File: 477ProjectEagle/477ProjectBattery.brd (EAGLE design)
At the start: 100 x 80 mm, 21 parts

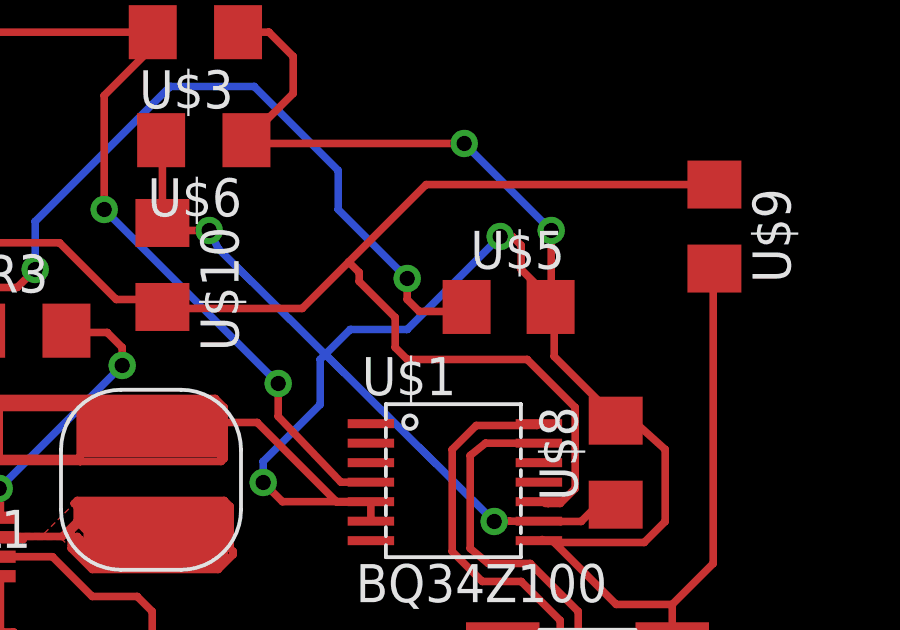
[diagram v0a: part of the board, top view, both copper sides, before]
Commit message: Made Major changes to the Battery PCB
I finished up the Battery PCB and incorporated the recommended layout
for the 3.3V source.
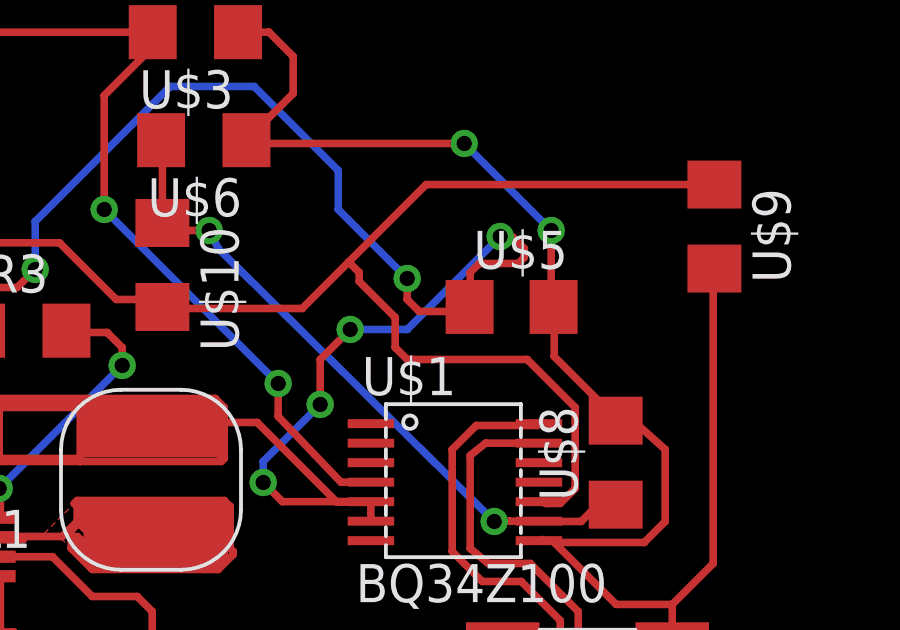
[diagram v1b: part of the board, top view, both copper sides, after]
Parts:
- moved U$5 0.10 mm to (58.6, 46.2)
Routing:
- net +3V3: track 134.6 -> 135.7 mm, vias 4 -> 6
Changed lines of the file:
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@@
 <element name="U$3" library="MinotaurParts" package="R1206" value="16k" x="48.04" y="55.41" rot="R180"/>
 <element name="U$4" library="MinotaurParts" package="R1206" value="240k" x="35.46" y="52.01" rot="R180"/>
-<element name="U$5" library="MinotaurParts" package="C1206" value="0.1uF" x="58.48" y="46.25"/>
+<element name="U$5" library="MinotaurParts" package="C1206" value="0.1uF" x="58.58" y="46.25"/>
 <element name="BATTERY" library="con-molex" package="22-23-2021" value="22-23-2021" x="55" y="25.14" rot="R180">
 <attribute name="OC_NEWARK" value="25C3832" x="35.95" y="42.92" size="1.778" layer="27" rot="R180" display="off"/>
@@
 <wire x1="50" y1="51.7" x2="57" y2="51.7" width="0.254" layer="1"/>
 <wire x1="57" y1="51.7" x2="59.9" y2="48.8" width="0.254" layer="16"/>
-<wire x1="59.9" y1="48.8" x2="59.9" y2="46.37" width="0.254" layer="1"/>
-<wire x1="59.9" y1="46.37" x2="59.88" y2="46.25" width="0.254" layer="1"/>
 <via x="57" y="51.7" extent="1-16" drill="0.508"/>
 <via x="59.9" y="48.8" extent="1-16" drill="0.508"/>
 <wire x1="62.1" y1="42.51" x2="62.09" y2="42.51" width="0.254" layer="1"/>
 <wire x1="62.09" y1="42.51" x2="60" y2="44.6" width="0.254" layer="1"/>
-<wire x1="60" y1="44.6" x2="60" y2="46.23" width="0.254" layer="1"/>
-<wire x1="60" y1="46.23" x2="59.88" y2="46.25" width="0.254" layer="1"/>
 <wire x1="60" y1="38.4" x2="63" y2="38.4" width="0.254" layer="1"/>
 <wire x1="63" y1="38.4" x2="63.7" y2="39.1" width="0.254" layer="1"/>
@@
 <wire x1="62.7" y1="42.4" x2="62.11" y2="42.4" width="0.254" layer="1"/>
 <wire x1="62.11" y1="42.4" x2="62.05" y2="42.46" width="0.254" layer="1"/>
-<wire x1="60" y1="38.4" x2="59.6" y2="38.5" width="0" layer="19" extent="1-1"/>
+<wire x1="60" y1="44.6" x2="60" y2="46.23" width="0.254" layer="1"/>
+<wire x1="60" y1="46.23" x2="59.98" y2="46.25" width="0.254" layer="1"/>
+<wire x1="59.6" y1="38.5" x2="60" y2="38.4" width="0" layer="19" extent="1-1"/>
 <wire x1="56.27" y1="25.14" x2="56.3" y2="24.2" width="0" layer="19" extent="1-1"/>
+<wire x1="59.9" y1="48.8" x2="59.9" y2="46.33" width="0.254" layer="1"/>
+<wire x1="59.9" y1="46.33" x2="59.98" y2="46.25" width="0.254" layer="1"/>
 </signal>
 <signal name="+3V3">
@@
 <contactref element="U$5" pad="1"/>
 <contactref element="3.3V_POWER" pad="1"/>
-<wire x1="59.95" y1="46.35" x2="60" y2="46.4" width="0.254" layer="1"/>
-<wire x1="60" y1="46.4" x2="60.1" y2="46.3" width="0.254" layer="1"/>
-<wire x1="57.08" y1="46.25" x2="57.08" y2="46.38" width="0.254" layer="1"/>
+<wire x1="59.95" y1="46.35" x2="60" y2="46.4" width="0" layer="19" extent="1-16"/>
+<wire x1="57.18" y1="46.25" x2="57.08" y2="46.38" width="0.254" layer="1"/>
 <wire x1="57.08" y1="46.38" x2="57.1" y2="46.4" width="0.254" layer="1"/>
 <wire x1="53.89" y1="39.11" x2="53.89" y2="39.76" width="0.254" layer="1"/>
@@
 <wire x1="55.1" y1="46.5" x2="55.5" y2="46.1" width="0.254" layer="1"/>
 <wire x1="55.5" y1="46.1" x2="56.93" y2="46.1" width="0.254" layer="1"/>
-<wire x1="56.93" y1="46.1" x2="57.08" y2="46.25" width="0.254" layer="1"/>
+<wire x1="56.93" y1="46.1" x2="57.18" y2="46.25" width="0.254" layer="1"/>
 <via x="42.7" y="47.5" extent="1-16" drill="0.508"/>
 <via x="55.1" y="47.2" extent="1-16" drill="0.508"/>
@@
 <wire x1="50.3" y1="40.4" x2="50.3" y2="41.1" width="0.254" layer="16"/>
 <wire x1="50.3" y1="41.1" x2="52.2" y2="43" width="0.254" layer="16"/>
-<wire x1="52.2" y1="43" x2="52.2" y2="44.5" width="0.254" layer="16"/>
-<wire x1="52.2" y1="44.5" x2="53.2" y2="45.5" width="0.254" layer="16"/>
+<wire x1="52.2" y1="43" x2="52.2" y2="44.5" width="0.254" layer="1"/>
+<wire x1="52.2" y1="44.5" x2="53.2" y2="45.5" width="0.254" layer="1"/>
 <wire x1="53.2" y1="45.5" x2="55.1" y2="45.5" width="0.254" layer="16"/>
 <wire x1="55.1" y1="45.5" x2="58.2" y2="48.6" width="0.254" layer="16"/>
 <wire x1="58.2" y1="48.6" x2="58.6" y2="48.6" width="0.254" layer="1"/>
-<wire x1="58.6" y1="48.6" x2="58.9" y2="48.3" width="0.254" layer="1"/>
-<wire x1="58.9" y1="48.3" x2="58.9" y2="47.5" width="0.254" layer="1"/>
-<wire x1="58.9" y1="47.5" x2="60" y2="46.4" width="0.254" layer="1"/>
 <via x="50.3" y="40.4" extent="1-16" drill="0.508"/>
 <via x="58.2" y="48.6" extent="1-16" drill="0.508"/>
+<via x="52.2" y="43" extent="1-16" drill="0.508"/>
+<via x="53.2" y="45.5" extent="1-16" drill="0.508"/>
+<wire x1="58.9" y1="48.3" x2="58.9" y2="47.5" width="0" layer="19" extent="1-16"/>
+<wire x1="58.9" y1="47.5" x2="60" y2="46.4" width="0" layer="19" extent="1-16"/>
+<wire x1="58.6" y1="48.6" x2="59" y2="48.2" width="0.254" layer="1"/>
+<wire x1="59" y1="48.2" x2="59" y2="47.9" width="0.254" layer="1"/>
+<wire x1="59" y1="47.9" x2="58.8" y2="47.7" width="0.254" layer="1"/>
+<wire x1="58.8" y1="47.7" x2="57.5" y2="47.7" width="0.254" layer="1"/>
+<wire x1="57.5" y1="47.7" x2="57.2" y2="47.4" width="0.254" layer="1"/>
+<wire x1="57.2" y1="47.4" x2="57.2" y2="46.3" width="0.254" layer="1"/>
+<wire x1="57.2" y1="46.3" x2="58.9" y2="48.3" width="0" layer="19" extent="1-16"/>
 </signal>
 <signal name="N$2">

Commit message: minor changes to main PCB
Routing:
- net GNDA: track 136.9 -> 138.0 mm
- added copper zone on layer 16, net GNDA
